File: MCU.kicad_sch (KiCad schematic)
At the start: 1 part, among them U1 STM32H745ZITx

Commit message: work in progress
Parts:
- added C28, C29: 2.2uF, Capacitor_SMD:C_0402_1005Metric_Pad0.74x0.62mm_HandSolder, symbol Device:C
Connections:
- net GND: now also U1.104 (VSS), U1.118 (VSS), U1.12 (VSS), U1.128 (VSS), U1.14 (VSSSMPS), U1.141 (VSS), U1.18 (VSS), U1.33 (VSS), U1.34 (VSSA), U1.41 (VSS), U1.55 (VSS), U1.6 (VSS), U1.69 (VSS), U1.80 (VSS), U1.89 (VSS), C28.2, C29.2
- net at U1.103 (VCAP): now also U1.140 (VCAP), U1.68 (VCAP), C28.1, C29.1
- net MCU Power/VDDLDO_1: now reaches U1.105 (VDDLDO)
- net MCU Power/VDD_9: now reaches U1.106 (VDD)
- net MCU Power/VDD_10: now reaches U1.119 (VDD)
- net MCU Power/VDD_11: now reaches U1.129 (VDD)
- net MCU Power/VDD_1: now reaches U1.13 (VDD)
- net MCU Power/VDDLDO_2: now reaches U1.143 (VDDLDO)
- net MCU Power/VDD_12: now reaches U1.144 (VDD)
- net MCU Power/VDDSMPS: now reaches U1.16 (VDDSMPS)
- net MCU Power/VDD_2: now reaches U1.19 (VDD)
- net MCU Power/VDD_3: now reaches U1.32 (VDD)
- net MCU Power/VDDA: now reaches U1.36 (VDDA)
- net MCU Power/VDD_4: now reaches U1.42 (VDD)
- net MCU Power/VDD_5: now reaches U1.56 (VDD)
- net MCU Power/VDD_0: now reaches U1.7 (VDD)
- net MCU Power/VDDLDO_0: now reaches U1.70 (VDDLDO)
- net MCU Power/VDD_6: now reaches U1.71 (VDD)
- net MCU Power/VDD_7: now reaches U1.79 (VDD)
- net MCU Power/VBAT: now reaches U1.8 (VBAT)
- net MCU Power/VDD50USB: now reaches U1.90 (VDD50_USB)
- net MCU Power/VDD33USB: now reaches U1.91 (VDD33_USB)
- net MCU Power/VDD_8: now reaches U1.92 (VDD)
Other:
- added sheet MCU Power (MCUPower.kicad_sch)
- moved on the sheet: U1

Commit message: worked on MII pinout
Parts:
- added C31: 220pF, Capacitor_SMD:C_0402_1005Metric_Pad0.74x0.62mm_HandSolder, symbol Device:C
- added C32: 10uF, Capacitor_SMD:C_0402_1005Metric_Pad0.74x0.62mm_HandSolder, symbol Device:C
- added L2: 2.2uH, symbol Device:L
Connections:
- net GND: now also C31.2, C32.2
- net at U1.15 (VLXSMPS): now also C31.1, L2.2
- net at U1.17 (VFBSMPS): now also C32.1
- net VREF+: now reaches U1.35 (VREF+)
- new net +3V3: L2.1
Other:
- sheet MCU Power ports: added VREF+; removed none
- moved on the sheet: C28, C29, U1

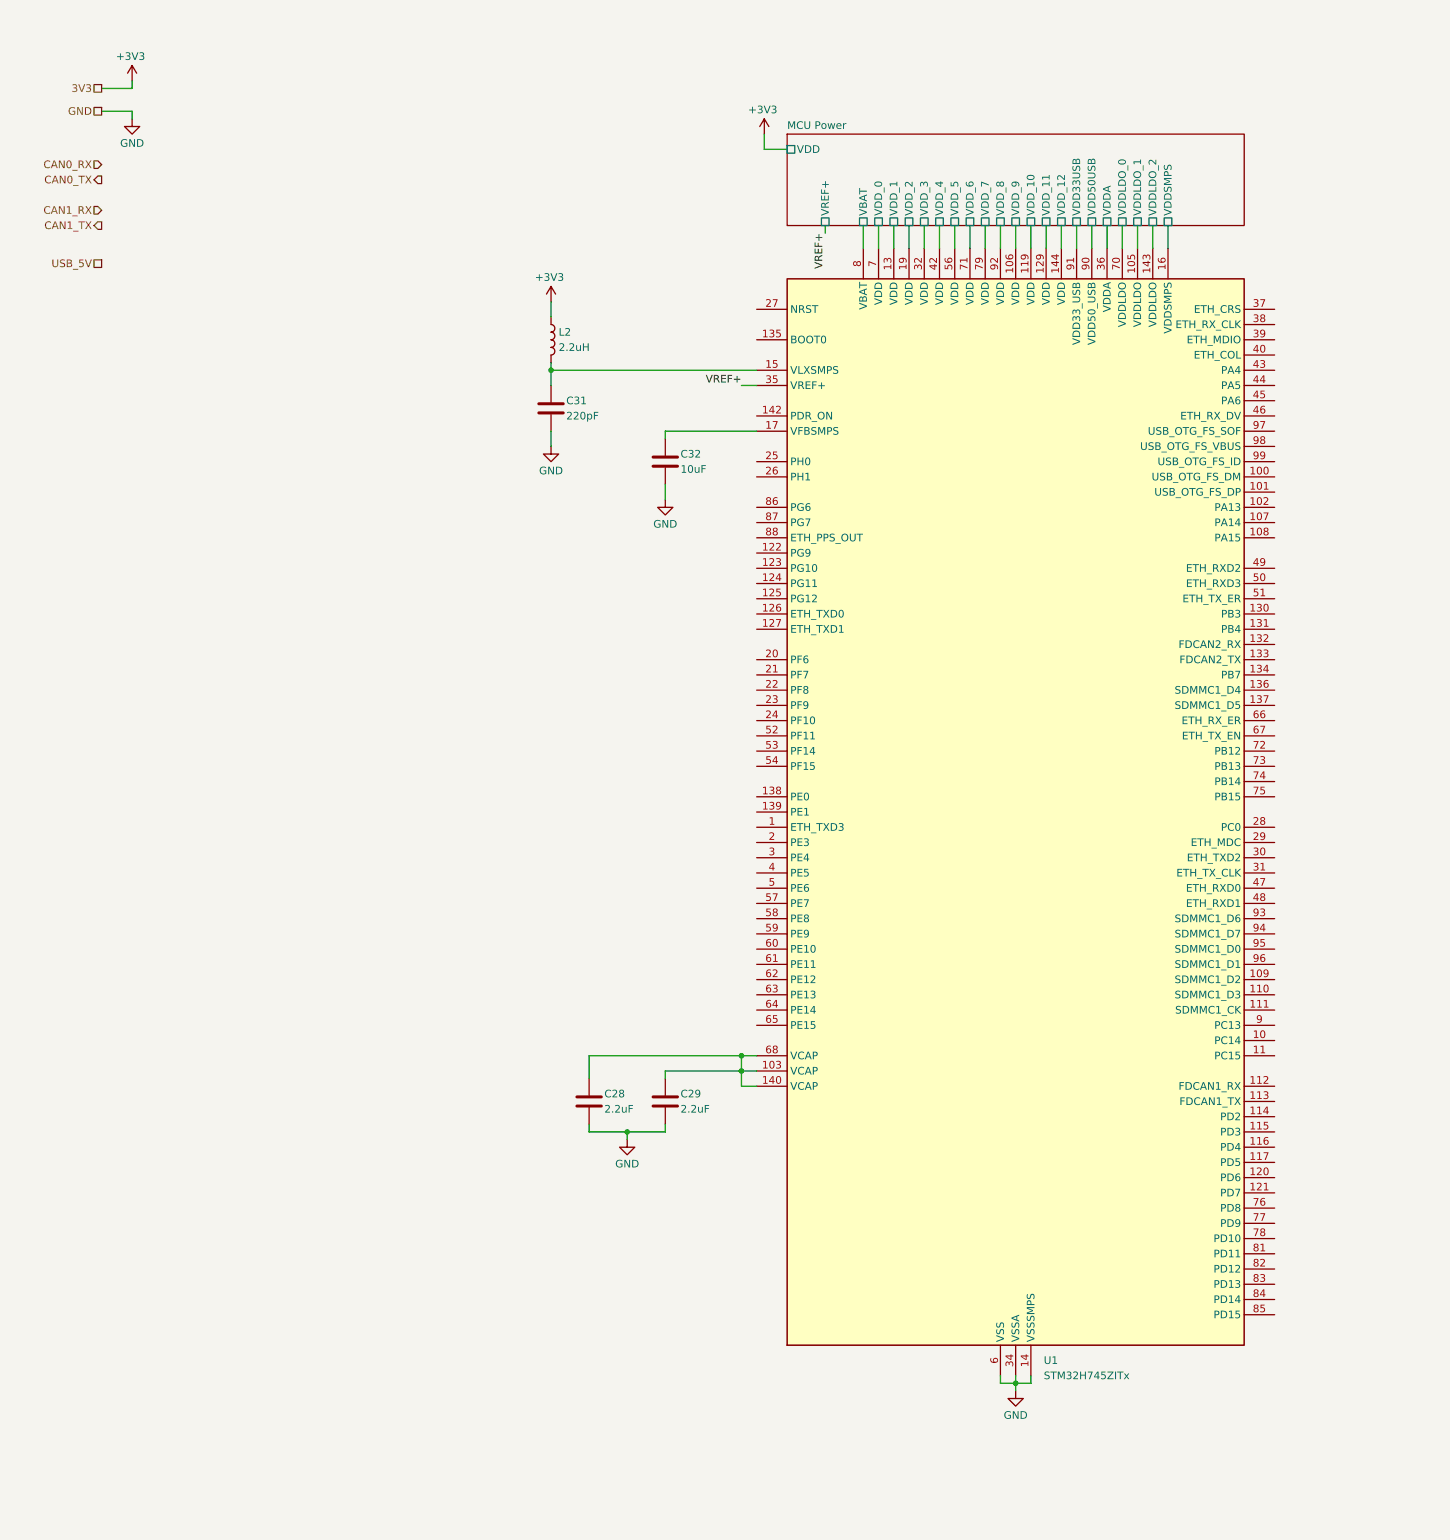
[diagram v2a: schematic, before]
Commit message: updated to use RMII and routed ethernet and CAN from micro
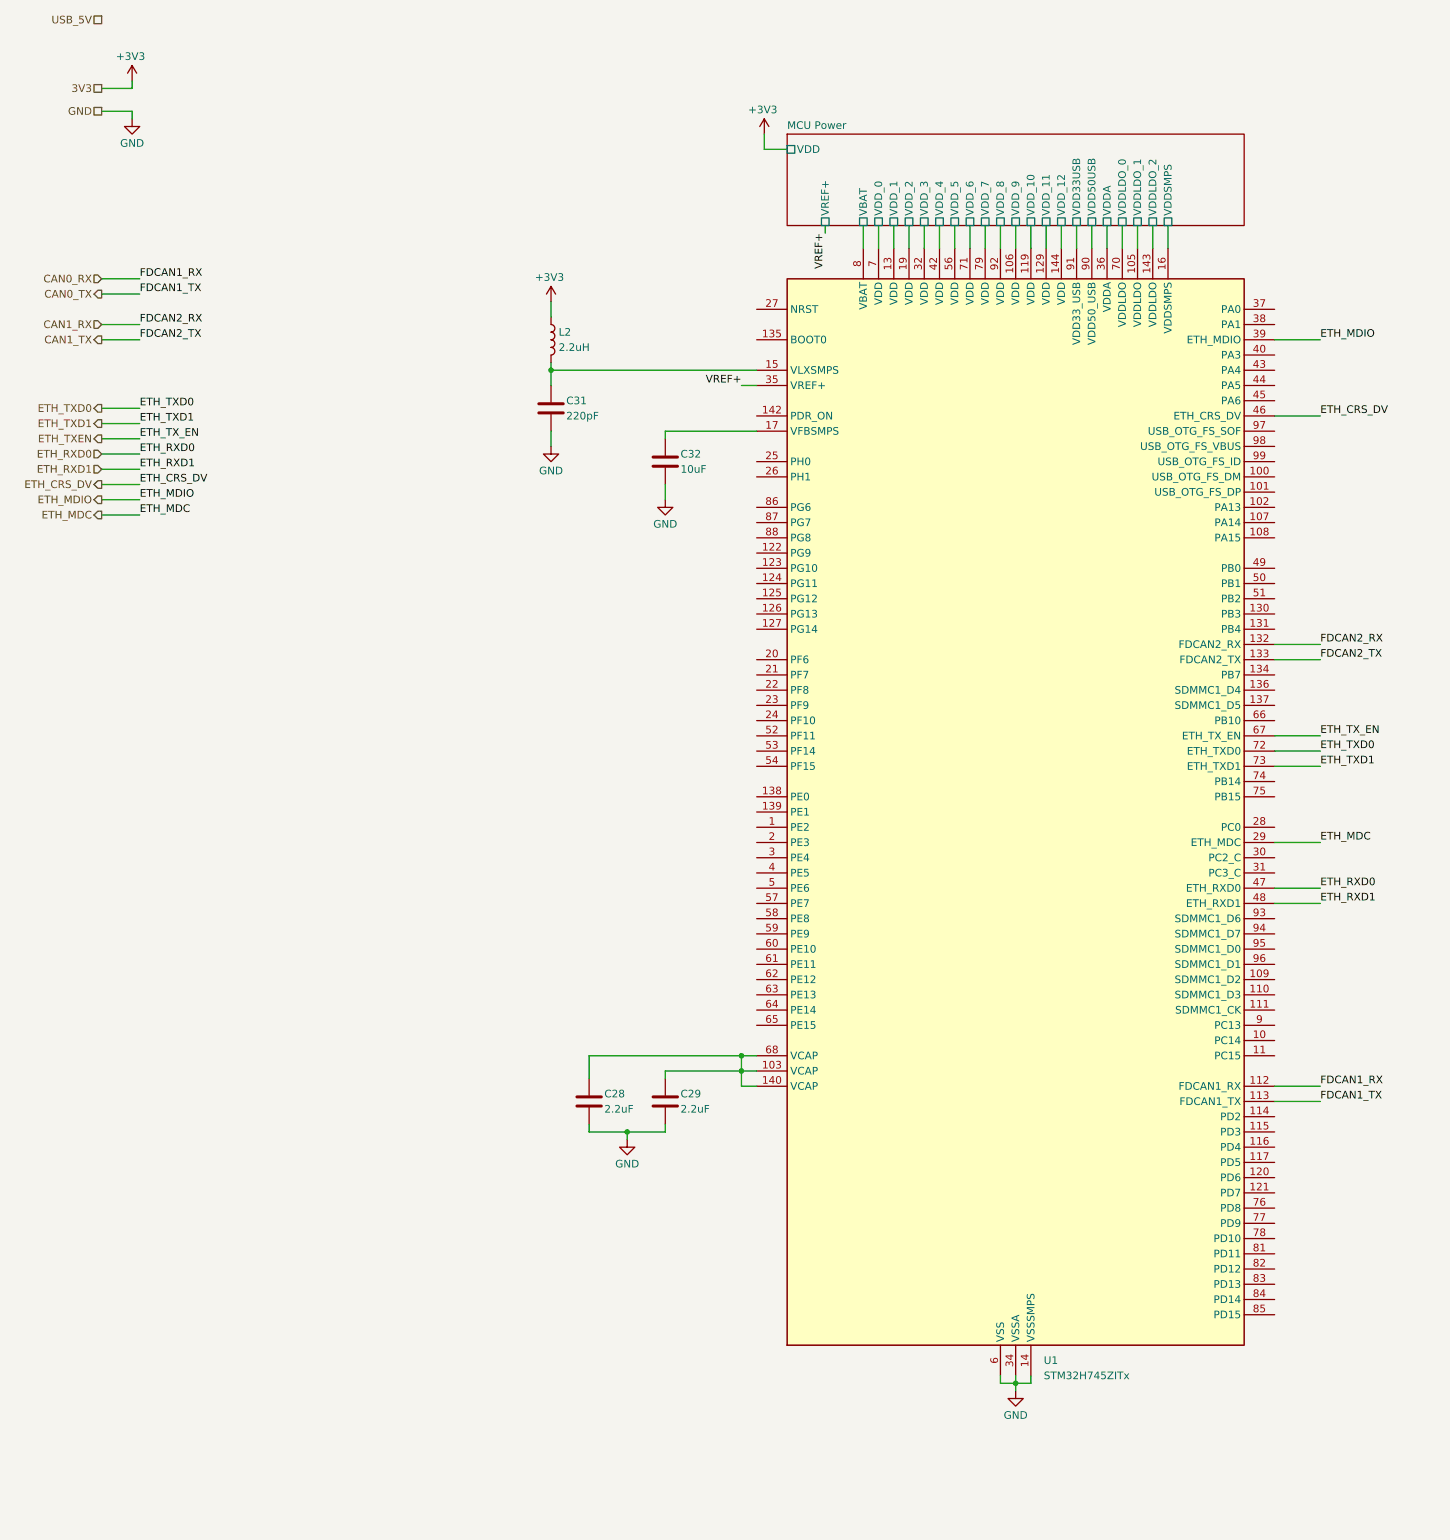
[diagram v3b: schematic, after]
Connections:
- net CAN0_RX: now also U1.112 (PD0)
- net CAN0_TX: now also U1.113 (PD1)
- net CAN1_RX: now also U1.132 (PB5)
- net CAN1_TX: now also U1.133 (PB6)
- net ETH_MDC: now reaches U1.29 (PC1)
- net ETH_MDIO: now reaches U1.39 (PA2)
- net ETH_CRS_DV: now reaches U1.46 (PA7)
- net ETH_RXD0: now reaches U1.47 (PC4)
- net ETH_RXD1: now reaches U1.48 (PC5)
- net ETH_TXEN: now reaches U1.67 (PB11)
- net ETH_TXD0: now reaches U1.72 (PB12)
- net ETH_TXD1: now reaches U1.73 (PB13)

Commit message: wip
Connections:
- net USB_DP: now reaches U1.100 (PA11)
- net USB_DM: now reaches U1.101 (PA12)
- net USB_VBUS: now reaches U1.98 (PA9)
- no-connect marks 0 -> 1
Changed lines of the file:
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@@
 		(color 0 0 0 0)
 	)
+	(no_connect
+		(at 220.98 88.9)
+	)
 	(wire
 		(pts
@@
 	(wire
 		(pts
+			(xy 31.75 114.3) (xy 25.4 114.3)
+		)
+		(stroke
+			(width 0)
+			(type default)
+		)
+	)
+	(wire
+		(pts
 			(xy 167.64 54.61) (xy 167.64 58.42)
 		)
@@
 	(wire
 		(pts
+			(xy 228.6 91.44) (xy 220.98 91.44)
+		)
+		(stroke
+			(width 0)
+			(type default)
+		)
+	)
+	(wire
+		(pts
+			(xy 228.6 96.52) (xy 220.98 96.52)
+		)
+		(stroke
+			(width 0)
+			(type default)
+		)
+	)
+	(wire
+		(pts
 			(xy 25.4 102.87) (xy 31.75 102.87)
 		)
@@
 	(wire
 		(pts
+			(xy 31.75 116.84) (xy 25.4 116.84)
+		)
+		(stroke
+			(width 0)
+			(type default)
+		)
+	)
+	(wire
+		(pts
 			(xy 25.4 71.12) (xy 31.75 71.12)
 		)
@@
 	(wire
 		(pts
+			(xy 31.75 119.38) (xy 25.4 119.38)
+		)
+		(stroke
+			(width 0)
+			(type default)
+		)
+	)
+	(wire
+		(pts
 			(xy 154.94 54.61) (xy 154.94 58.42)
+		)
+		(stroke
+			(width 0)
+			(type default)
+		)
+	)
+	(wire
+		(pts
+			(xy 228.6 99.06) (xy 220.98 99.06)
 		)
 		(stroke
@@
 		)
 	)
+	(label "USB_OTG_FS_VBUS"
+		(at 228.6 91.44 0)
+		(effects
+			(font
+				(size 1.27 1.27)
+			)
+			(justify left bottom)
+		)
+	)
 	(label "ETH_MDIO"
 		(at 228.6 73.66 0)
@@
 		)
 	)
+	(label "USB_OTG_FS_DP"
+		(at 228.6 99.06 0)
+		(effects
+			(font
+				(size 1.27 1.27)
+			)
+			(justify left bottom)
+		)
+	)
 	(label "ETH_MDC"
 		(at 228.6 157.48 0)
@@
 		)
 	)
+	(label "USB_OTG_FS_DP"
+		(at 31.75 116.84 0)
+		(effects
+			(font
+				(size 1.27 1.27)
+			)
+			(justify left bottom)
+		)
+	)
 	(label "FDCAN1_TX"
 		(at 228.6 200.66 0)
@@
 		)
 	)
+	(label "USB_OTG_FS_DM"
+		(at 31.75 114.3 0)
+		(effects
+			(font
+				(size 1.27 1.27)
+			)
+			(justify left bottom)
+		)
+	)
 	(label "VREF+"
 		(at 146.05 55.88 270)
@@
 		)
 	)
+	(label "USB_OTG_FS_VBUS"
+		(at 31.75 119.38 0)
+		(effects
+			(font
+				(size 1.27 1.27)
+			)
+			(justify left bottom)
+		)
+	)
 	(label "FDCAN2_TX"
 		(at 31.75 73.66 0)
@@
 	(label "ETH_MDC"
 		(at 31.75 102.87 0)
+		(effects
+			(font
+				(size 1.27 1.27)
+			)
+			(justify left bottom)
+		)
+	)
+	(label "USB_OTG_FS_DM"
+		(at 228.6 96.52 0)
 		(effects
 			(font
@@
 		)
 	)
+	(hierarchical_label "USB_DP"
+		(shape bidirectional)
+		(at 25.4 114.3 180)
+		(effects
+			(font
+				(size 1.27 1.27)
+			)
+			(justify right)
+		)
+	)
+	(hierarchical_label "USB_VBUS"
+		(shape passive)
+		(at 25.4 119.38 180)
+		(effects
+			(font
+				(size 1.27 1.27)
+			)
+			(justify right)
+		)
+	)
 	(hierarchical_label "ETH_TXEN"
 		(shape output)
@@
 		(effects
 			(font
+				(size 1.27 1.27)
+			)
+			(justify right)
+		)
+	)
+	(hierarchical_label "USB_DM"
+		(shape bidirectional)
+		(at 25.4 116.84 180)
+		(effects
+			(font

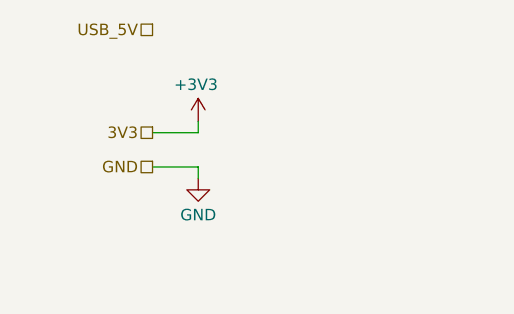
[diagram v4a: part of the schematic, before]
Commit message: full initial power scheme
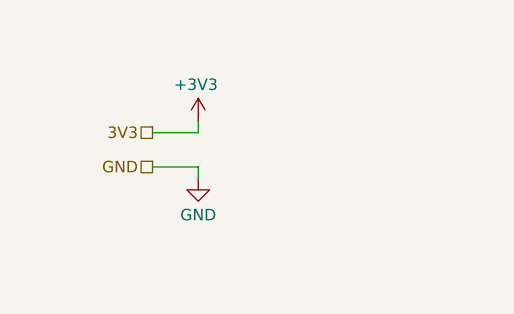
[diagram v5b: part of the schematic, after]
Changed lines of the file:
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@@
-		)
-	)
-	(hierarchical_label "USB_5V"
-		(shape passive)
-		(at 25.4 20.32 180)
-		(effects
-			(font
-				(size 1.27 1.27)
-			)
-			(justify right)
 		)
 	)
